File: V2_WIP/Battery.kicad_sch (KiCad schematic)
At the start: 22 parts, among them J601 BATT, SW601 MSN22AFW01, U601 IP5306, U602 STC3100IST

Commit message: added USB, button
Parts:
- J601: footprint 1769:1769 -> Connector_Molex:Molex_PicoBlade_53398-0271_1x02-1MP_P1.25mm_Vertical
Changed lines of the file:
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@@
 			)
 		)
-		(property "Datasheet" ""
+		(property "Datasheet" "https://www.laskakit.cz/user/related_files/ip5306-1.pdf"
 			(at 78.74 95.25 0)
 			(effects
@@
 			)
 		)
-		(property "Datasheet" ""
+		(property "Datasheet" "https://www.st.com/resource/en/datasheet/stc3100.pdf"
 			(at 173.99 111.76 0)
 			(effects
@@
 			)
 		)
-		(property "Footprint" "1769:1769"
+		(property "Footprint" "Connector_Molex:Molex_PicoBlade_53398-0271_1x02-1MP_P1.25mm_Vertical"
 			(at 241.3 91.44 0)
 			(effects
@@
 			)
 		)
-		(property "Datasheet" "~"
+		(property "Datasheet" "https://cz.mouser.com/ProductDetail/Molex/53398-4004?qs=iLbezkQI%252Bsg1CAiQuTsV2g%3D%3D"
 			(at 241.3 91.44 0)
 			(effects

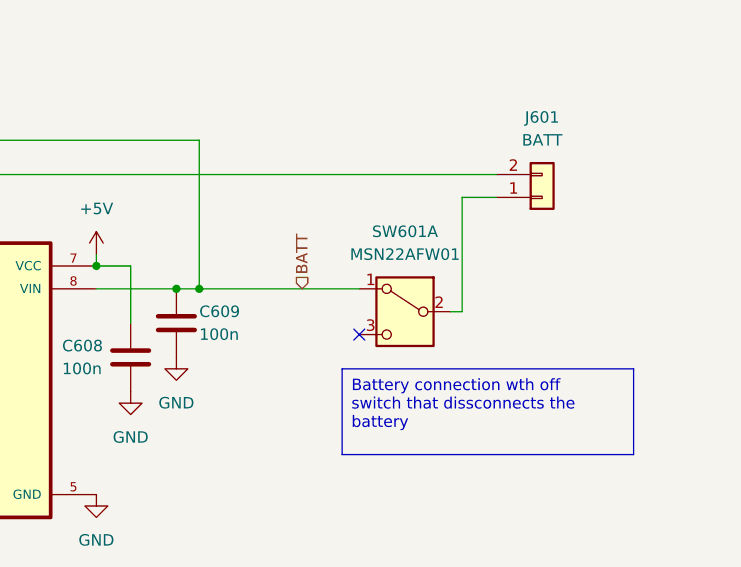
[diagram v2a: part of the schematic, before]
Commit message: fixed errors in schematic
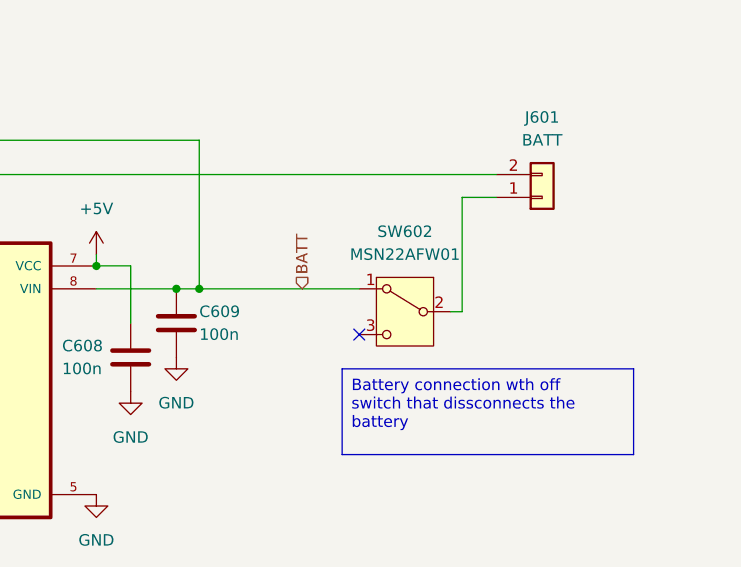
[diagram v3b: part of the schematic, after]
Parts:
- removed SW601: MSN22AFW01, Button_Switch_THT:MSN22AFW01, symbol Switch:SW_DPDT_x2
- added SW602: MSN22AFW01, Button_Switch_THT:MSN22AFW01, symbol Switch:SW_SPDT
- R_E601, R_E602, R_E603, R_E604: footprint Resistor_SMD:R_0805_2012Metric_Pad1.20x1.40mm_HandSolder -> Resistor_SMD:R_0603_1608Metric_Pad0.98x0.95mm_HandSolder
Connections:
- net BATT: now also SW602.1 (A)
- net at J601.1 (Pin_1): now also SW602.2 (B)
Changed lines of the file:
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@@
+	)
+	(symbol
+		(lib_id "Switch:SW_SPDT")
+		(at 226.06 104.14 0)
+		(mirror y)
+		(unit 1)
+		(exclude_from_sim no)
+		(in_bom yes)
+		(on_board yes)
+		(dnp no)
+		(property "Reference" "SW602"
+			(at 226.06 95.25 0)
+			(effects
+				(font
+					(size 1.27 1.27)
+				)
+			)
+		)
+		(property "Value" "MSN22AFW01"
+			(at 226.06 97.79 0)
+			(effects
+				(font
+					(size 1.27 1.27)
+				)
+			)
+		)
+		(property "Footprint" "Button_Switch_THT:MSN22AFW01"
+			(at 226.06 104.14 0)
+			(effects
+				(font
+					(size 1.27 1.27)
+				)
+				(hide yes)
+			)
+		)
+		(property "Datasheet" "https://cz.mouser.com/datasheet/2/295/MSN_SlidesNonillum_DP-3450118.pdf"
+			(at 226.06 111.76 0)
+			(effects
+				(font
+					(size 1.27 1.27)
+				)
+				(hide yes)
+			)
+		)
+		(property "Description" "Switch, single pole double throw"
+			(at 226.06 104.14 0)
+			(effects
+				(font
+					(size 1.27 1.27)
+				)
+				(hide yes)
+			)
+		)
+		(pin "3"
+		)
+		(pin "2"
+		)
+		(pin "1"
+		)
+		(instances
+			(project ""
+				(path "/00526ddc-5304-4072-af1e-192a9e7e83da/280f742a-a734-4c07-ab96-9dbf73329b01"
+					(reference "SW602")
+					(unit 1)
+				)
+			)
+		)
 	)
 	(symbol
@@
 			)
 		)
-		(property "Footprint" "Resistor_SMD:R_0805_2012Metric_Pad1.20x1.40mm_HandSolder"
+		(property "Footprint" "Resistor_SMD:R_0603_1608Metric_Pad0.98x0.95mm_HandSolder"
 			(at 147.828 128.27 90)
 			(effects
@@
 	)
 	(symbol
-		(lib_id "Switch:SW_DPDT_x2")
-		(at 226.06 104.14 0)
-		(mirror y)
-		(unit 1)
-		(exclude_from_sim no)
-		(in_bom yes)
-		(on_board yes)
-		(dnp no)
-		(fields_autoplaced yes)
-		(property "Reference" "SW601"
-			(at 226.06 95.25 0)
-			(effects
-				(font
-					(size 1.27 1.27)
-				)
-			)
-		)
-		(property "Value" "MSN22AFW01"
-			(at 226.06 97.79 0)
-			(effects
-				(font
-					(size 1.27 1.27)
-				)
-			)
-		)
-		(property "Footprint" "Button_Switch_THT:MSN22AFW01"
-			(at 226.06 104.14 0)
-			(effects
-				(font
-					(size 1.27 1.27)
-				)
-				(hide yes)
-			)
-		)
-		(property "Datasheet" "https://cz.mouser.com/datasheet/2/295/MSN_SlidesNonillum_DP-3450118.pdf"
-			(at 226.06 104.14 0)
-			(effects
-				(font
-					(size 1.27 1.27)
-				)
-				(hide yes)
-			)
-		)
-		(property "Description" "Switch, dual pole double throw, separate symbols"
-			(at 226.06 104.14 0)
-			(effects
-				(font
-					(size 1.27 1.27)
-				)
-				(hide yes)
-			)
-		)
-		(pin "3"
-		)
-		(pin "2"
-		)
-		(pin "1"
-		)
-		(pin "4"
-		)
-		(pin "5"
-		)
-		(pin "6"
-		)
-		(instances
-			(project "gps"
-				(path "/00526ddc-5304-4072-af1e-192a9e7e83da/280f742a-a734-4c07-ab96-9dbf73329b01"
-					(reference "SW601")
-					(unit 1)
-				)
-			)
-		)
-	)
-	(symbol
 		(lib_id "power:GND")
 		(at 191.77 124.46 0)
@@
 			)
 		)
-		(property "Footprint" "Resistor_SMD:R_0805_2012Metric_Pad1.20x1.40mm_HandSolder"
+		(property "Footprint" "Resistor_SMD:R_0603_1608Metric_Pad0.98x0.95mm_HandSolder"
 			(at 44.958 83.82 90)
 			(effects
@@
 			)
 		)
-		(property "Footprint" "Resistor_SMD:R_0805_2012Metric_Pad1.20x1.40mm_HandSolder"
+		(property "Footprint" "Resistor_SMD:R_0603_1608Metric_Pad0.98x0.95mm_HandSolder"
 			(at 113.538 114.3 90)
 			(effects
@@
 			)
 		)
-		(property "Footprint" "Resistor_SMD:R_0805_2012Metric_Pad1.20x1.40mm_HandSolder"
+		(property "Footprint" "Resistor_SMD:R_0603_1608Metric_Pad0.98x0.95mm_HandSolder"
 			(at 51.308 96.52 90)
 			(effects

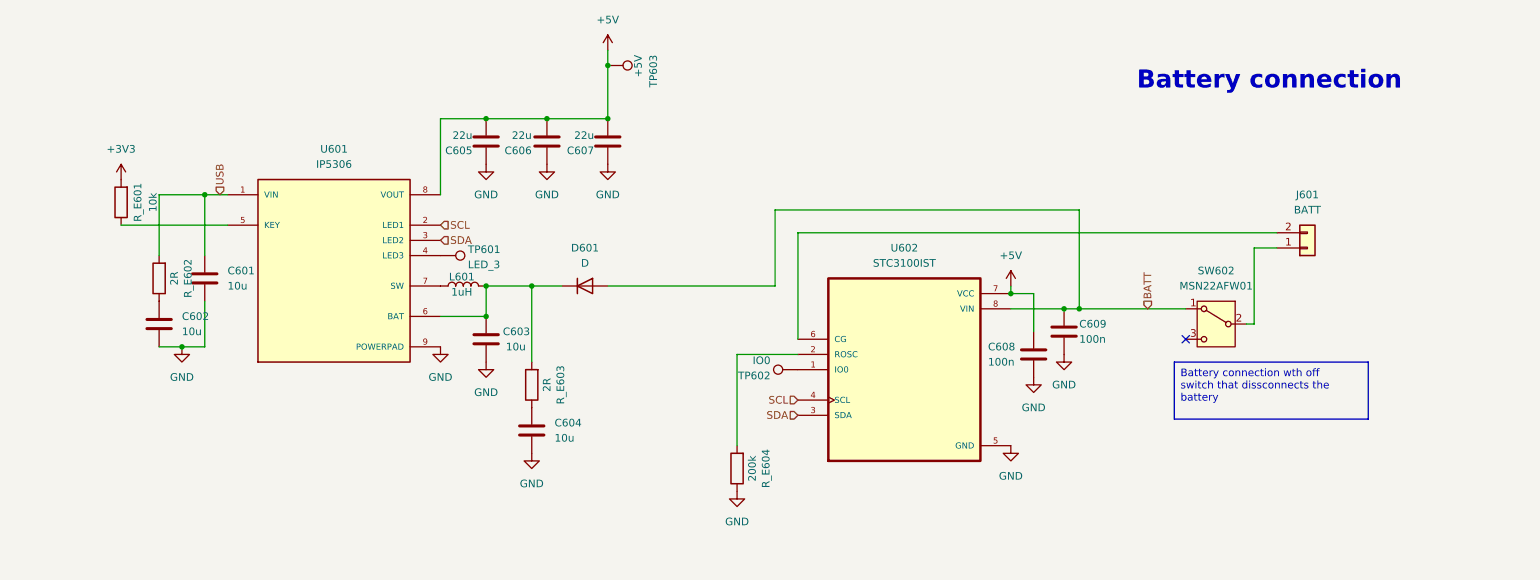
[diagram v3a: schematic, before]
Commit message: Removed EEPROM, Adjusted Flash connection, renamed ESP pins and several other signals
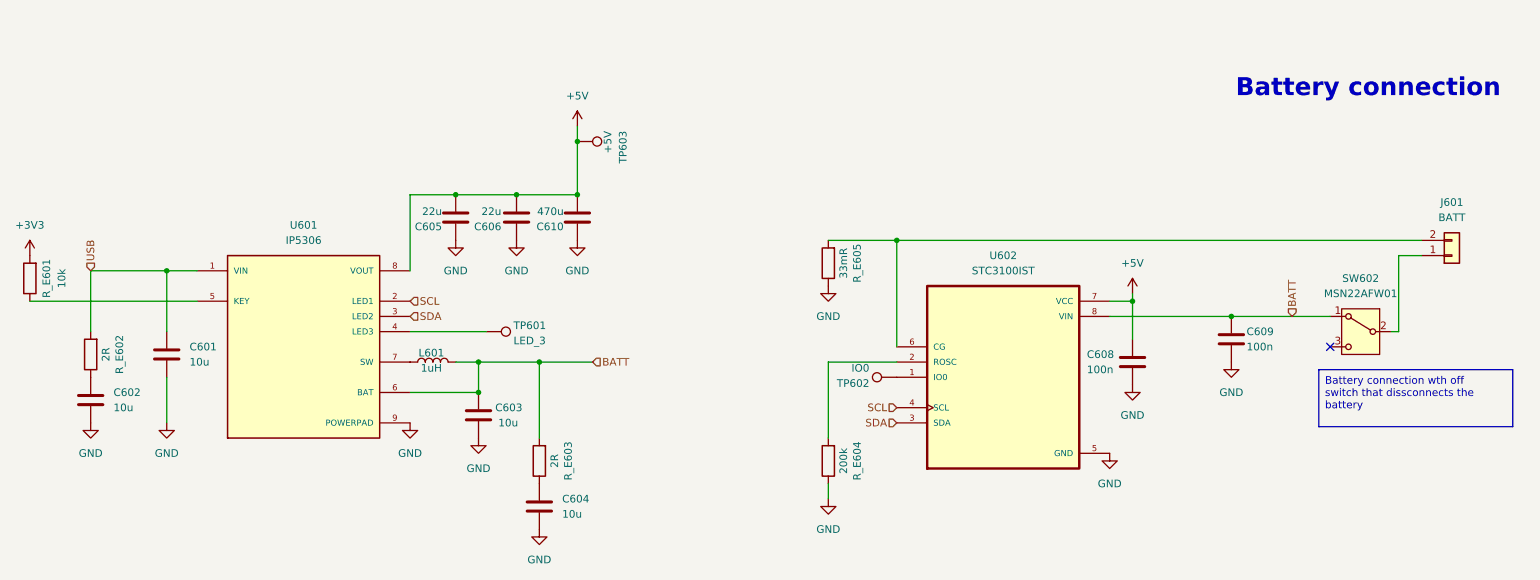
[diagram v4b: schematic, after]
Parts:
- removed C607: 22u, Capacitor_SMD:C_0603_1608Metric_Pad1.08x0.95mm_HandSolder, symbol Device:C
- removed D601: D, Diode_SMD:D_0603_1608Metric_Pad1.05x0.95mm_HandSolder, symbol Device:D
- added C610: 470u, Capacitor_SMD:C_0603_1608Metric_Pad1.08x0.95mm_HandSolder, symbol Device:C
- added R_E605: 33mR, Resistor_SMD:R_0603_1608Metric_Pad0.98x0.95mm_HandSolder, symbol Device:R
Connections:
- net +5V: now also C610.2
- net BATT: now also C603.1, L601.2, R_E603.2, U601.6 (BAT)
- net GND: now also C610.1, R_E605.1
- net at J601.2 (Pin_2), U602.6 (CG): now also R_E605.2
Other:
- moved on the sheet: C601, C602, C603, C604, C605, C606, C608, C609, J601, L601, R_E601, R_E602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

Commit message: minor changes
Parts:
- removed C606: 22u, Capacitor_SMD:C_0603_1608Metric_Pad1.08x0.95mm_HandSolder, symbol Device:C
- added C606: 10u, Capacitor_Tantalum_SMD:CP_EIA-3528-15_AVX-H_Pad1.50x2.35mm_HandSolder, symbol Device:C_Polarized
- C610: footprint Capacitor_SMD:C_0603_1608Metric_Pad1.08x0.95mm_HandSolder -> Capacitor_SMD:C_Elec_6.3x7.7
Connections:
- net +5V: now also C606.1
- net GND: now also C606.2

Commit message: finallizes schematic; pcb progress
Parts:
- removed C610: 470u, Capacitor_SMD:C_Elec_6.3x7.7, symbol Device:C
- removed TP603: +5V, TestPoint:TestPoint_Pad_D1.5mm, symbol Connector:TestPoint
- added C610: C_Polarized, Capacitor_SMD:C_Elec_6.3x7.7, symbol Device:C_Polarized
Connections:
- net +5V: now also C610.1
- net GND: now also C610.2
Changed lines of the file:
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@@
+	)
+	(junction
+		(at 119.38 82.55)
+		(diameter 0)
+		(color 0 0 0 0)
 	)
 	(junction
@@
 		(color 0 0 0 0)
 	)
-	(junction
-		(at 119.38 82.55)
-		(diameter 0)
-		(color 0 0 0 0)
-	)
-	(junction
-		(at 119.38 73.66)
-		(diameter 0)
-		(color 0 0 0 0)
-	)
 	(no_connect
 		(at 245.11 107.95)
@@
 	(wire
 		(pts
-			(xy 119.38 73.66) (xy 119.38 82.55)
+			(xy 119.38 80.01) (xy 119.38 82.55)
 		)
 		(stroke
@@
 		)
 	)
-	(wire
-		(pts
-			(xy 119.38 71.12) (xy 119.38 73.66)
-		)
-		(stroke
-			(width 0)
-			(type default)
-		)
-	)
-	(text_box "Battery connection wth off switch that dissconnects the battery"
+	(text_box "MaxOut 2A"
+		(exclude_from_sim no)
+		(at 98.044 65.532 0)
+		(size 11.176 5.08)
+		(stroke
+			(width 0)
+			(type default)
+		)
+		(fill
+			(type none)
+		)
+		(effects
+			(font
+				(size 1.27 1.27)
+			)
+			(justify left top)
+		)
+	)
+	(text_box "Battery connection with off switch that disconnects the battery"
 		(exclude_from_sim no)
 		(at 243.205 111.76 0)
@@
 	)
 	(symbol
-		(lib_id "Connector:TestPoint")
-		(at 119.38 73.66 270)
-		(unit 1)
-		(exclude_from_sim no)
-		(in_bom yes)
-		(on_board yes)
-		(dnp no)
-		(property "Reference" "TP603"
-			(at 127 71.882 0)
-			(effects
-				(font
-					(size 1.27 1.27)
-				)
-				(justify left)
-			)
-		)
-		(property "Value" "+5V"
-			(at 124.46 71.882 0)
-			(effects
-				(font
-					(size 1.27 1.27)
-				)
-				(justify left)
-			)
-		)
-		(property "Footprint" "TestPoint:TestPoint_Pad_D1.5mm"
-			(at 119.38 78.74 0)
-			(effects
-				(font
-					(size 1.27 1.27)
-				)
-				(hide yes)
-			)
-		)
-		(property "Datasheet" "~"
-			(at 119.38 78.74 0)
-			(effects
-				(font
-					(size 1.27 1.27)
-				)
-				(hide yes)
-			)
-		)
-		(property "Description" "test point"
-			(at 119.38 73.66 0)
-			(effects
-				(font
-					(size 1.27 1.27)
-				)
-				(hide yes)
-			)
-		)
-		(pin "1"
-		)
-		(instances
-			(project "gps"
-				(path "/00526ddc-5304-4072-af1e-192a9e7e83da/280f742a-a734-4c07-ab96-9dbf73329b01"
-					(reference "TP603")
-					(unit 1)
-				)
-			)
-		)
-	)
-	(symbol
 		(lib_id "power:+3V3")
 		(at 27.94 92.71 0)
@@
 	(symbol
 		(lib_id "power:+5V")
-		(at 119.38 71.12 0)
+		(at 119.38 80.01 0)
 		(unit 1)
 		(exclude_from_sim no)
@@
 		(fields_autoplaced yes)
 		(property "Reference" "#PWR0601"
+			(at 119.38 83.82 0)
+			(effects
+				(font
+					(size 1.27 1.27)
+				)
+				(hide yes)
+			)
+		)
+		(property "Value" "+5V"
 			(at 119.38 74.93 0)
 			(effects
@@
 					(size 1.27 1.27)
 				)
-				(hide yes)
-			)
-		)
-		(property "Value" "+5V"
-			(at 119.38 66.04 0)
-			(effects
-				(font
-					(size 1.27 1.27)
-				)
 			)
 		)
 		(property "Footprint" ""
-			(at 119.38 71.12 0)
+			(at 119.38 80.01 0)
 			(effects
 				(font
@@
 		)
 		(property "Datasheet" ""
-			(at 119.38 71.12 0)
+			(at 119.38 80.01 0)
 			(effects
 				(font
@@
 		)
 		(property "Description" "Power symbol creates a global label with name \"+5V\""
-			(at 119.38 71.12 0)
+			(at 119.38 80.01 0)
 			(effects
 				(font
@@
 	)
 	(symbol
-		(lib_id "Device:C")
-		(at 119.38 86.36 180)
-		(unit 1)
-		(exclude_from_sim no)
-		(in_bom yes)
-		(on_board yes)
-		(dnp no)
-		(property "Reference" "C610"
-			(at 117.094 87.884 0)
-			(effects
-				(font
-					(size 1.27 1.27)
-				)
-				(justify left)
-			)
-		)
-		(property "Value" "470u"
-			(at 117.094 85.344 0)
-			(effects
-				(font
-					(size 1.27 1.27)
-				)
-				(justify left)
-			)
-		)
-		(property "Footprint" "Capacitor_SMD:C_Elec_6.3x7.7"
-			(at 118.4148 82.55 0)
-			(effects
-				(font
-					(size 1.27 1.27)
-				)
-				(hide yes)
-			)
-		)
-		(property "Datasheet" "~"
-			(at 119.38 86.36 0)
-			(effects
-				(font
-					(size 1.27 1.27)
-				)
-				(hide yes)
-			)
-		)
-		(property "Description" "Unpolarized capacitor"
-			(at 119.38 86.36 0)
-			(effects
-				(font
-					(size 1.27 1.27)
-				)
-				(hide yes)
-			)
-		)
-		(pin "1"
-		)
-		(pin "2"
-		)
-		(instances
-			(project "gps"
-				(path "/00526ddc-5304-4072-af1e-192a9e7e83da/280f742a-a734-4c07-ab96-9dbf73329b01"
-					(reference "C610")
-					(unit 1)
-				)
-			)
-		)
-	)
-	(symbol
 		(lib_id "power:GND")
 		(at 208.28 125.73 0)
@@
 					(unit 1)
 				)
+			)
+		)
+	)
+	(symbol
+		(lib_id "Device:C_Polarized")
+		(at 119.38 86.36 0)
+		(unit 1)
+		(exclude_from_sim no)
+		(in_bom yes)
+		(on_board yes)
+		(dnp no)
+		(fields_autoplaced yes)
+		(property "Reference" "C610"
+			(at 123.19 84.2009 0)
+			(effects
+				(font
+					(size 1.27 1.27)
+				)
+				(justify left)
+			)
+		)
+		(property "Value" "C_Polarized"
+			(at 123.19 86.7409 0)
+			(effects
+				(font
+					(size 1.27 1.27)
+				)
+				(justify left)
+			)
+		)
+		(property "Footprint" "Capacitor_SMD:C_Elec_6.3x7.7"
+			(at 120.3452 90.17 0)
+			(effects
+				(font
+					(size 1.27 1.27)
+				)
+				(hide yes)
+			)
+		)
+		(property "Datasheet" "~"
+			(at 119.38 86.36 0)
+			(effects
+				(font
+					(size 1.27 1.27)
+				)
+				(hide yes)
+			)
+		)
+		(property "Description" "Polarized capacitor"
+			(at 119.38 86.36 0)
+			(effects
+				(font
+					(size 1.27 1.27)
+				)
+				(hide yes)
+			)
+		)
+		(pin "1"
+		)
+		(pin "2"
+		)
+		(instances
+			(project ""
+				(path "/00526ddc-5304-4072-af1e-192a9e7e83da/280f742a-a734-4c07-ab96-9dbf73329b01"
+					(reference "C610")
+					(unit 1)
+				)

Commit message: updated most datashets
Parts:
- C601, C602, C603, C604: value 10u -> 10uF
- C605: value 22u -> 22uF
- C606: value 10u -> *10uF
- C608, C609: value 100n -> 100nF
- C610: value C_Polarized -> 470uF
- L601: value 1uH -> *1uH
- U601: value IP5306 -> *IP5306
